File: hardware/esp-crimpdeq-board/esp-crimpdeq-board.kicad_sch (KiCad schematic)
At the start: 64 parts, among them J1 USB4105-GF-A, Q1 DMG3415U, SW1 SW_Push, SW2 SW_Push, U1 SHTC3, U2 ICM-42670-P, U3 ESP32-C3-MINI-1, U4 SY8088, U5 HX711, U6 MCP73831T-2ACI/OT, Y1 32.768Hz

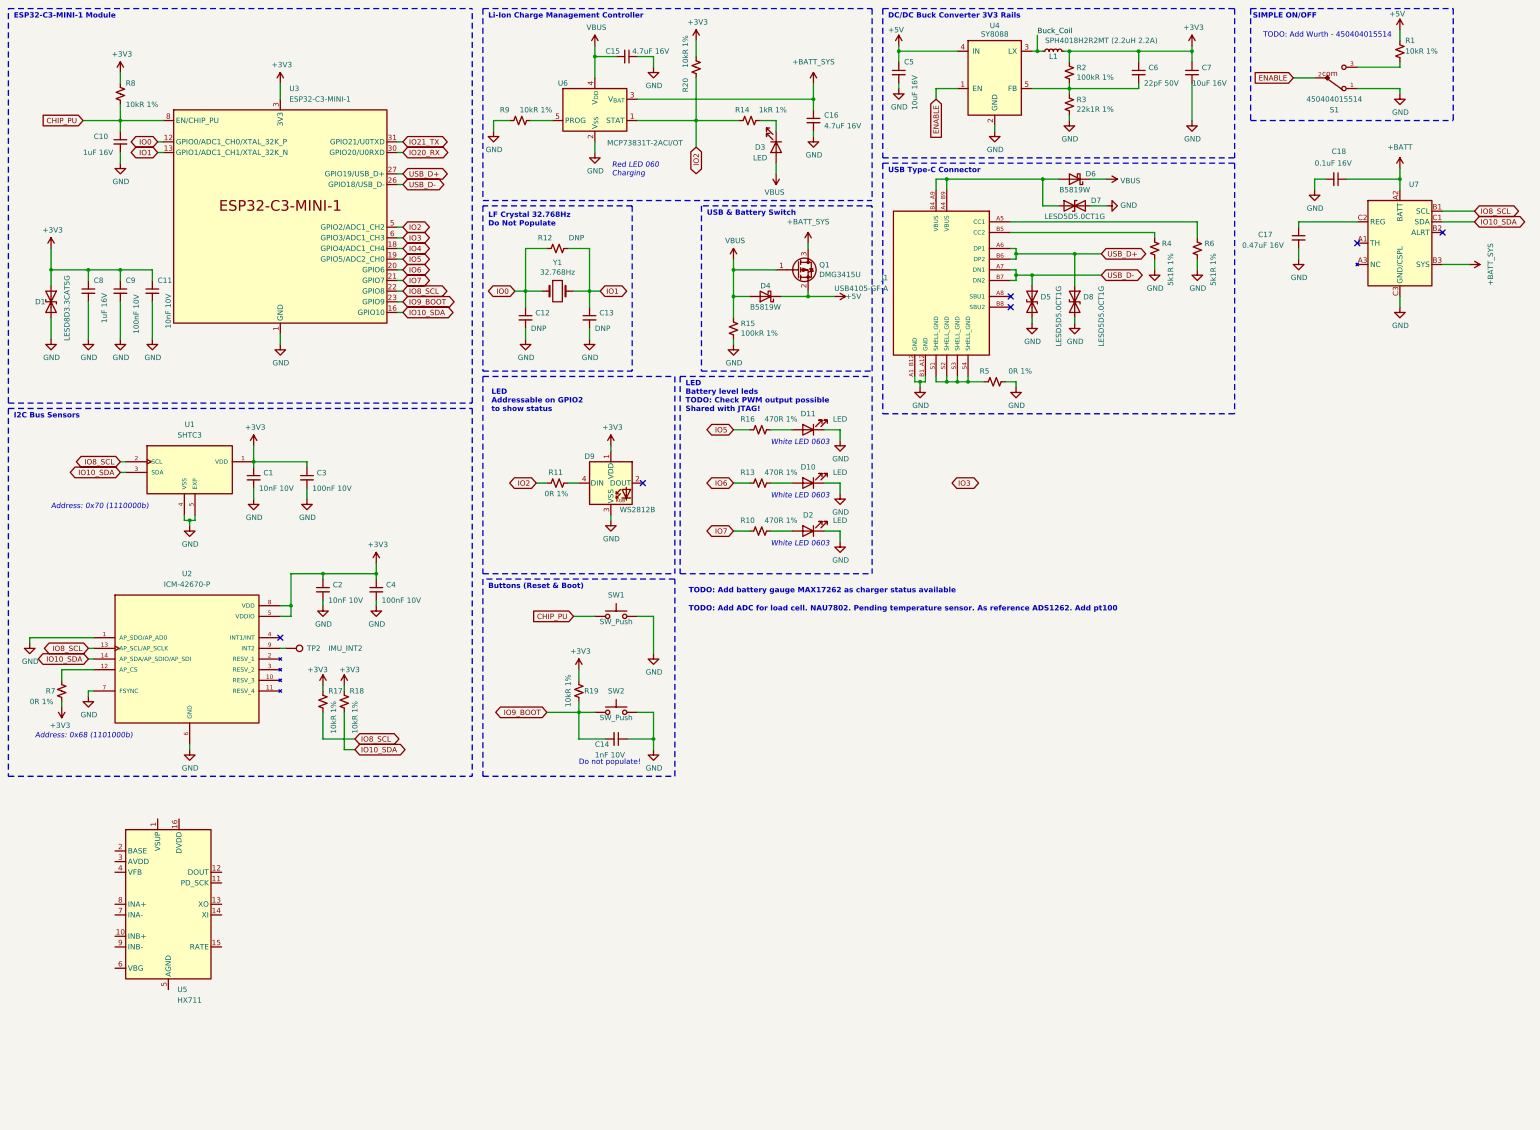
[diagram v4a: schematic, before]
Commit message: ADC updated
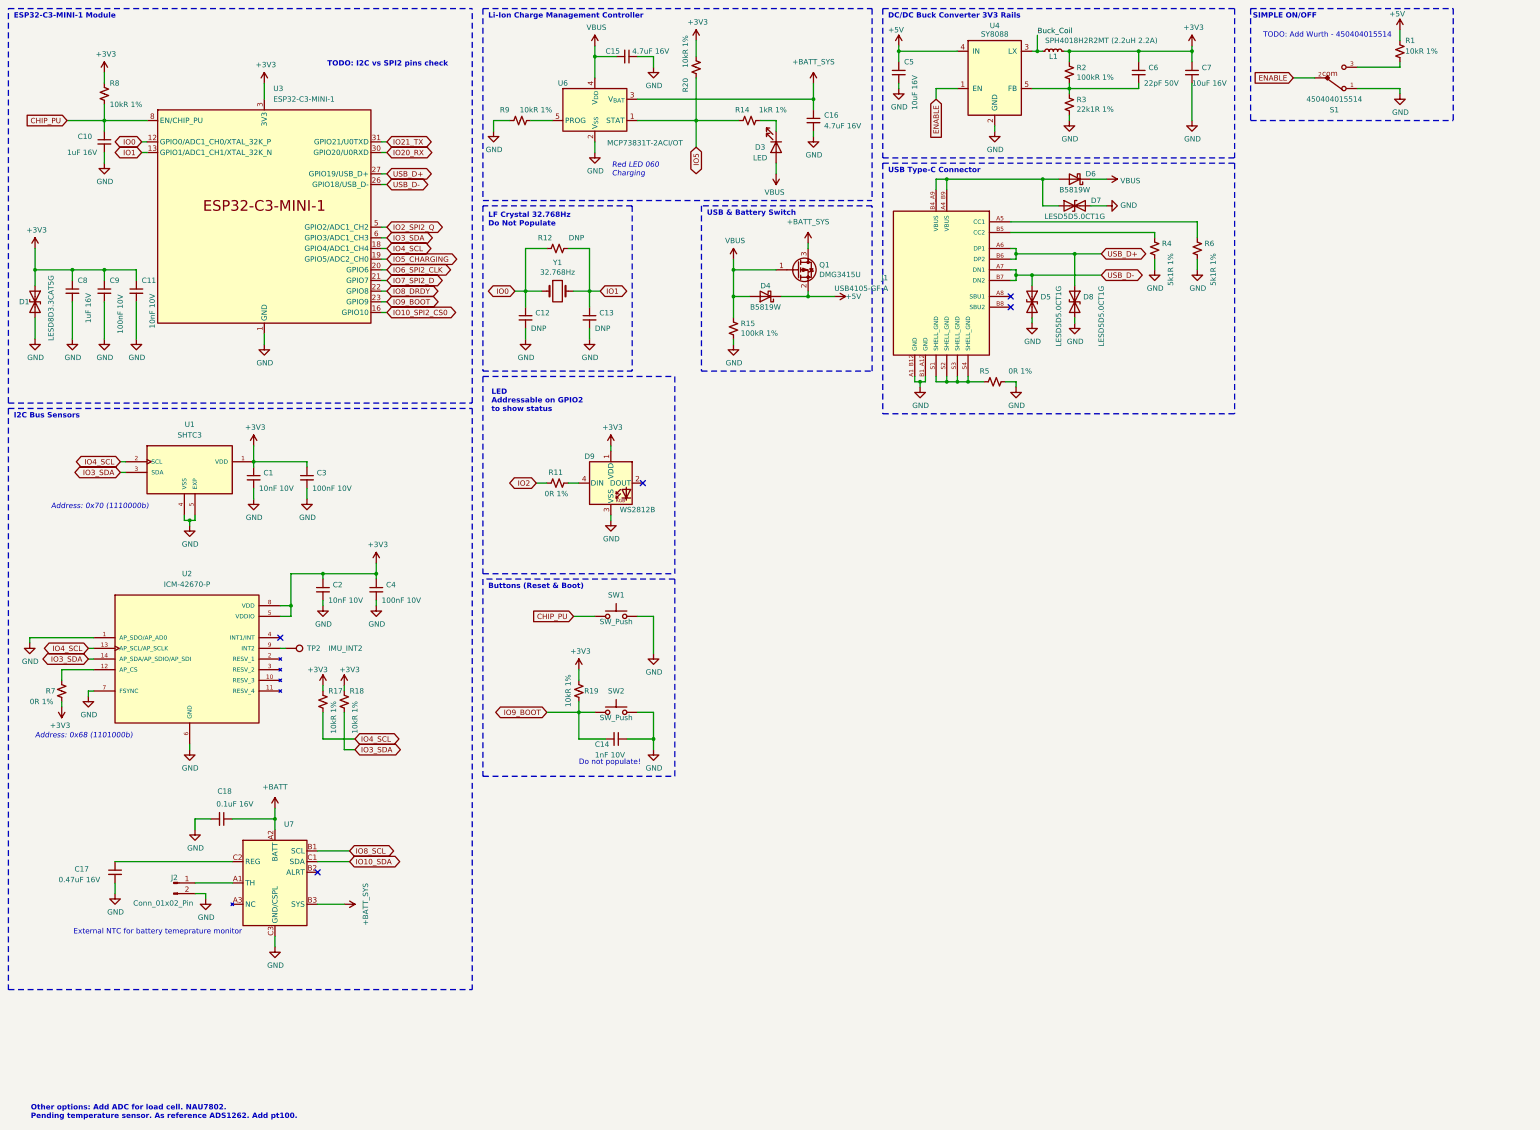
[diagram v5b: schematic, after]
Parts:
- removed D10, D11, D2: LED, LED_SMD:LED_0603_1608Metric, symbol Device:LED
- removed R10, R13, R16: 470R 1%, Resistor_SMD:R_0402_1005Metric, symbol Device:R_Small_US
- removed U5: HX711, Package_SO:SOP-16_3.9x9.9mm_P1.27mm, symbol Analog_ADC:HX711
- added J2: Conn_01x02_Pin, symbol Connector:Conn_01x02_Pin
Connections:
- net GND: now also J2.2 (Pin_2)
- net IO10_SDA: no longer R18.2, U1.3 (SDA), U2.14 (AP_SDA/AP_SDIO/AP_SDI), U3.16 (GPIO10)
- net IO2: no longer R14.1, R20.1, U3.5 (GPIO2/ADC1_CH2), U6.1 (STAT)
- net IO5: now also R14.1, R20.1, U6.1 (STAT); no longer U3.19 (GPIO5/ADC2_CH0)
- net IO8_SCL: no longer R17.2, U1.2 (SCL), U2.13 (AP_SCL/AP_SCLK), U3.22 (GPIO8)
- net at U7.A1 (TH): now also J2.1 (Pin_1)
- net IO3 renamed IO3_SDA
- net IO3_SDA: now also R18.2, U1.3 (SDA), U2.14 (AP_SDA/AP_SDIO/AP_SDI)
- net IO4 renamed IO4_SCL
- net IO4_SCL: now also R17.2, U1.2 (SCL), U2.13 (AP_SCL/AP_SCLK)
- net IO6 renamed IO6_SPI2_CLK
- net IO7 renamed IO7_SPI2_D
- new net IO10_SPI2_CS0: U3.16 (GPIO10)
- new net IO2_SPI2_Q: U3.5 (GPIO2/ADC1_CH2)
- new net IO5_CHARGING: U3.19 (GPIO5/ADC2_CH0)
- new net IO8_DRDY: U3.22 (GPIO8)
- no-connect marks 6 -> 5
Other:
- note added: "External NTC for battery temeprature monitor"
- note added: "Other options: Add ADC for load cell. NAU7802. Pending temperature sensor. As reference ADS1262. Add pt100."
- note added: "TODO: I2C vs SPI2 pins check"
- note removed: "LED Battery level leds TODO: Check PWM output possible Shared with JTAG!"
- note removed: "TODO: Add ADC for load cell. NAU7802. Pending temperature sensor. As reference ADS1262. Add pt100"
- note removed: "TODO: Add battery gauge MAX17262 as charger status available"
- note removed: "White LED 0603"
- moved on the sheet: C10, C11, C17, C18, C8, C9, D1, R8, U3, U7

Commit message: Changed micro
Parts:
- removed U3: ESP32-C3-MINI-1, PCM_Espressif:ESP32-C3-MINI-1, symbol PCM_Espressif:ESP32-C3-MINI-1
- added C19: 680pF 10V, Capacitor_SMD:C_0402_1005Metric, symbol Device:C_Small
- added C20, C21: 0.1uF 10V, Capacitor_SMD:C_0402_1005Metric, symbol Device:C_Small
- added R10, R13: 47R 0.1%, Resistor_SMD:R_0402_1005Metric, symbol Device:R_Small_US
- added U5: NAU7802SGI, Package_SO:SOP-16_3.9x9.9mm_P1.27mm, symbol Nuvoton:NAU7802SGI
- added U8: ESP32-C6-MINI-1/U, PCM_Espressif:ESP32-C6-MINI-1, symbol PCM_Espressif:ESP32-C6-MINI-1/U
- U7: value ~ -> MAX17262
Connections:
- net +3V3: now also U8.3 (3V3)
- net CHIP_PU: now also U8.8 (EN/CHIP_PU)
- net GND: now also C21.2, U5.7 (REFN), U5.8 (AVSS), U5.9 (DVSS), U8.1 (GND), U8.11 (GND), U8.14 (GND), U8.2 (GND), U8.36 (GND), U8.37 (GND), U8.38 (GND), U8.39 (GND), U8.40 (GND), U8.41 (GND), U8.42 (GND), U8.43 (GND), U8.44 (GND), U8.45 (GND), U8.46 (GND), U8.47 (GND), U8.48 (GND), U8.49 (GND), U8.50 (GND), U8.51 (GND), U8.52 (GND), U8.53 (GND)
- net IO0: now also U8.12 (GPIO0/ADC1_CH0/XTAL_32K_P)
- net IO1: now also U8.13 (GPIO1/ADC1_CH1/XTAL_32K_N)
- net IO10_SPI2_CS0: now also U8.29 (GPIO23)
- net IO20_RX: now also U8.30 (U0RXD/GPIO17)
- net IO21_TX: now also U8.31 (U0TXD/GPIO16)
- net IO2_SPI2_Q: now also U8.19 (GPIO14)
- net IO3_SDA: now also U8.22 (GPIO8)
- net IO4_SCL: now also U8.24 (GPIO18)
- net IO5_CHARGING: now also U8.25 (GPIO19)
- net IO6_SPI2_CLK: now also U8.26 (GPIO20)
- net IO7_SPI2_D: now also U8.27 (GPIO21)
- net IO8_DRDY: now also U8.28 (GPIO22)
- net IO9_BOOT: now also U8.23 (GPIO9)
- net USB_D+: now also U8.18 (GPIO13/USB_D+)
- net USB_D-: now also U8.17 (GPIO12/USB_D-)
- new net: C21.1, U5.1 (REFP), U5.16 (AVDD/LDO)
- new net: C19.1, U5.5 (VIN2P)
- new net: C19.2, U5.4 (VIN2N)
- new net: C20.2, R13.2, U5.2 (VIN1N)
- new net: C20.1, R10.2, U5.3 (VIN1P)
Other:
- note added: "ADS1235 is avery good technical option but overkilling budget"
- note added: "Pending temperature sensor. As reference ADS1262. Add pt100."
- note added: "TODO: Add voltage regulator form 3.3 to 5 V"
- note removed: "Other options: Add ADC for load cell. NAU7802. Pending temperature sensor. As reference ADS1262. Add pt100."
- moved on the sheet: C10, C11, C8, C9, D1, R8

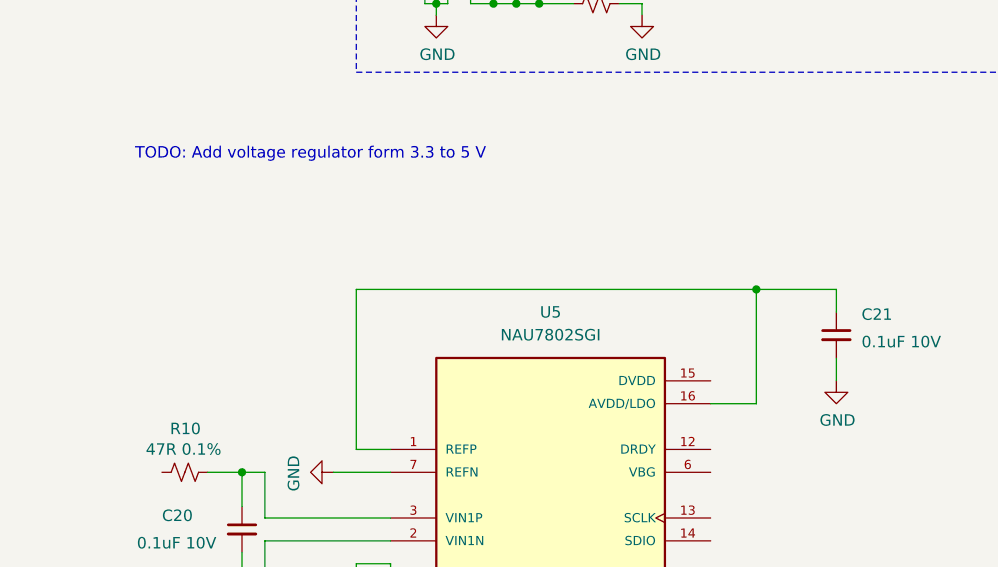
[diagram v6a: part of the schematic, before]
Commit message: Cahnged uC
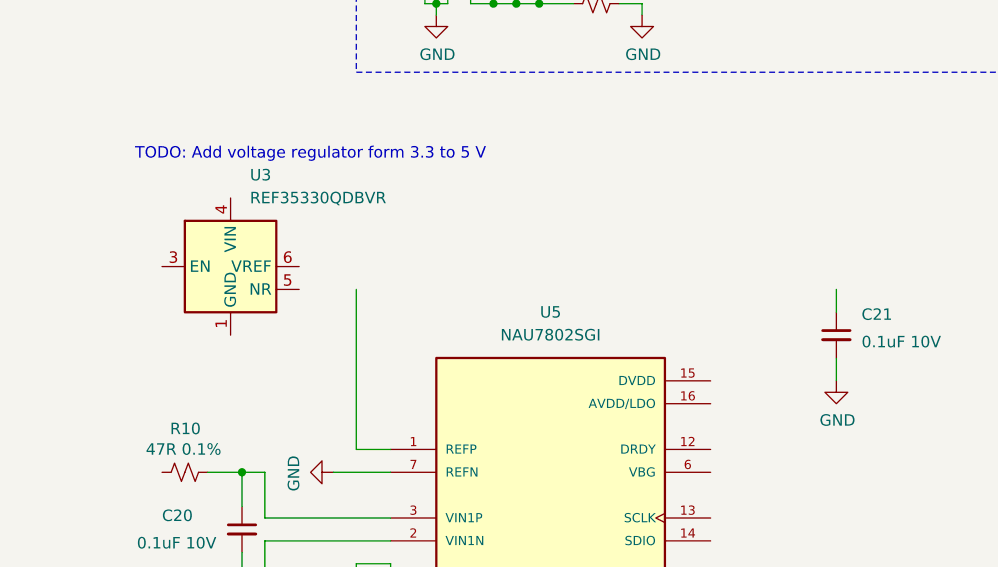
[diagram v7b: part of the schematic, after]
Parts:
- added U3: REF35330QDBVR, Package_TO_SOT_SMD:SOT-23-6, symbol Reference_Voltage:REF35330QDBVR
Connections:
- new net: U3.1 (GND), U3.2 (GND)
- now unconnected: C21.1, U5.1 (REFP), U5.16 (AVDD/LDO)
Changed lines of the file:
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@@
 	)
 	(junction
-		(at 265.43 134.62)
-		(diameter 0)
-		(color 0 0 0 0)
-	)
-	(junction
 		(at 236.22 54.61)
 		(diameter 0)
@@
 	(wire
 		(pts
-			(xy 265.43 134.62) (xy 274.32 134.62)
-		)
-		(stroke
-			(width 0)
-			(type default)
-		)
-	)
-	(wire
-		(pts
 			(xy 71.12 118.11) (xy 71.12 121.92)
 		)
@@
 	(wire
 		(pts
-			(xy 220.98 134.62) (xy 265.43 134.62)
-		)
-		(stroke
-			(width 0)
-			(type default)
-		)
-	)
-	(wire
-		(pts
 			(xy 295.91 64.77) (xy 295.91 68.58)
 		)
@@
 	(wire
 		(pts
-			(xy 265.43 134.62) (xy 265.43 147.32)
-		)
-		(stroke
-			(width 0)
-			(type default)
-		)
-	)
-	(wire
-		(pts
 			(xy 87.63 181.61) (xy 87.63 187.96)
 		)
@@
 	(wire
 		(pts
-			(xy 265.43 147.32) (xy 260.35 147.32)
-		)
-		(stroke
-			(width 0)
-			(type default)
-		)
-	)
-	(wire
-		(pts
 			(xy 76.2 204.47) (xy 76.2 207.01)
 		)
@@
 					(unit 1)
 				)
+			)
+		)
+	)
+	(symbol
+		(lib_id "Reference_Voltage:REF35330QDBVR")
+		(at 207.01 132.08 0)
+		(unit 1)
+		(exclude_from_sim no)
+		(in_bom yes)
+		(on_board yes)
+		(dnp no)
+		(fields_autoplaced yes)
+		(property "Reference" "U3"
+			(at 209.1533 121.92 0)
+			(effects
+				(font
+					(size 1.27 1.27)
+				)
+				(justify left)
+			)
+		)
+		(property "Value" "REF35330QDBVR"
+			(at 209.1533 124.46 0)
+			(effects
+				(font
+					(size 1.27 1.27)
+				)
+				(justify left)
+			)
+		)
+		(property "Footprint" "Package_TO_SOT_SMD:SOT-23-6"
+			(at 207.01 153.67 0)
+			(effects
+				(font
+					(size 1.27 1.27)
+				)
+				(hide yes)
+			)
+		)
+		(property "Datasheet" "https://www.ti.com/lit/ds/symlink/ref35.pdf"
+			(at 207.01 151.13 0)
+			(effects
+				(font
+					(size 1.27 1.27)
+				)
+				(hide yes)
+			)
+		)
+		(property "Description" "3.3V, Ultra Low-Power, High-Precision Voltage Reference, SOT-23-6"
+			(at 207.01 113.03 0)
+			(effects
+				(font
+					(size 1.27 1.27)
+				)
+				(hide yes)
+			)
+		)
+		(pin "2"
+		)
+		(pin "6"
+		)
+		(pin "5"
+		)
+		(pin "3"
+		)
+		(pin "4"
+		)
+		(pin "1"
+		)
+		(instances
+			(project ""
+				(path "/196a8dd5-5fd6-4c7f-ae4a-0104bd82e61b"
+					(reference "U3")
+					(unit 1)
+				)

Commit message: + work
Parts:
- added C22, C24: 0.1uF 10V, Capacitor_SMD:C_0402_1005Metric, symbol Device:C_Small
- added C23, C25: 1uF 16V, Capacitor_SMD:C_0402_1005Metric, symbol Device:C_Small
- added R21, R22, R23: 10kR 1%, Resistor_SMD:R_0402_1005Metric, symbol Device:R_Small_US
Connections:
- net +3V3: now also R21.1, R22.1, R23.2
- net +5V: now also U3.4 (VIN), C22.1, C23.1
- net GND: now also U3.1 (GND), U3.2 (GND), C22.2, C23.2, C24.2, C25.2
- net IO3_SDA: now also U5.14 (SDIO); no longer U1.3 (SDA)
- net IO4_SCL: now also U5.13 (SCLK); no longer U1.2 (SCL)
- net at U3.3 (EN): now also R23.1
- net VREF3V3: now reaches U3.6 (VREF)
- net VREF3V3: now also U5.1 (REFP), C24.1, C25.1
- net IO10_SDA renamed IOX_LP_SDA
- net IOX_LP_SDA: now also U1.3 (SDA), R22.2
- net IO8_SCL renamed IOX_LP_SCL
- net IOX_LP_SCL: now also U1.2 (SCL), R21.2
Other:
- note removed: "ADS1235 is avery good technical option but overkilling budget"
- note removed: "TODO: Add voltage regulator form 3.3 to 5 V"
